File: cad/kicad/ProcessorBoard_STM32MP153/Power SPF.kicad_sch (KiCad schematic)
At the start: 8 parts

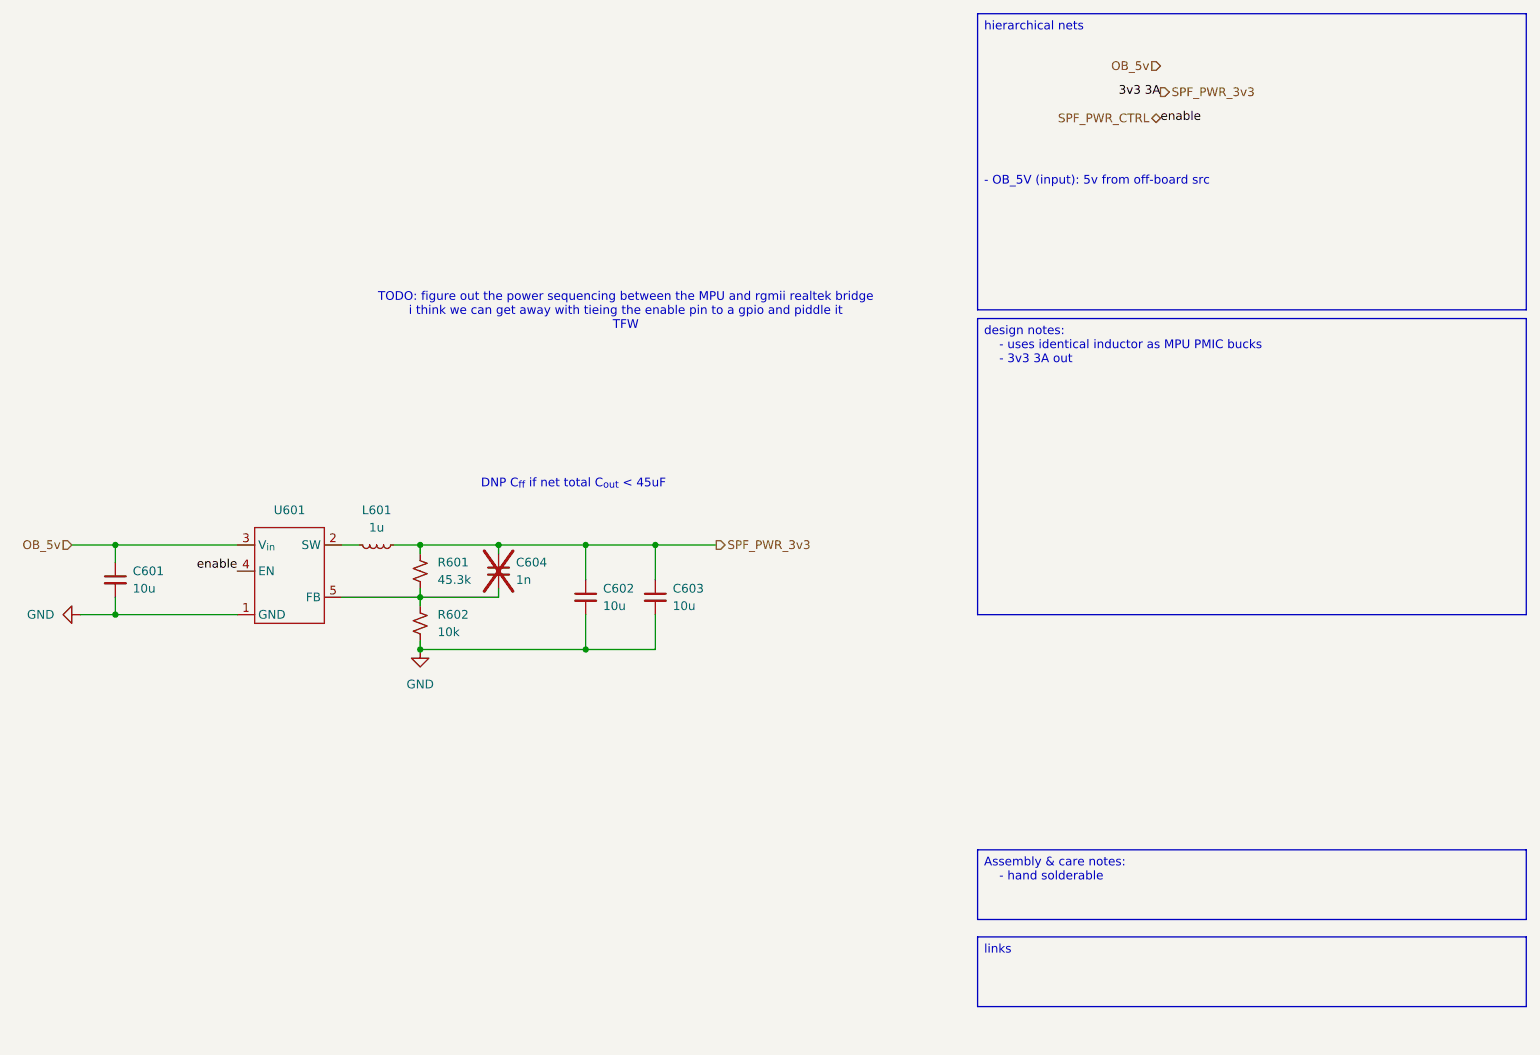
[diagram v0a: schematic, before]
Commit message: new ram
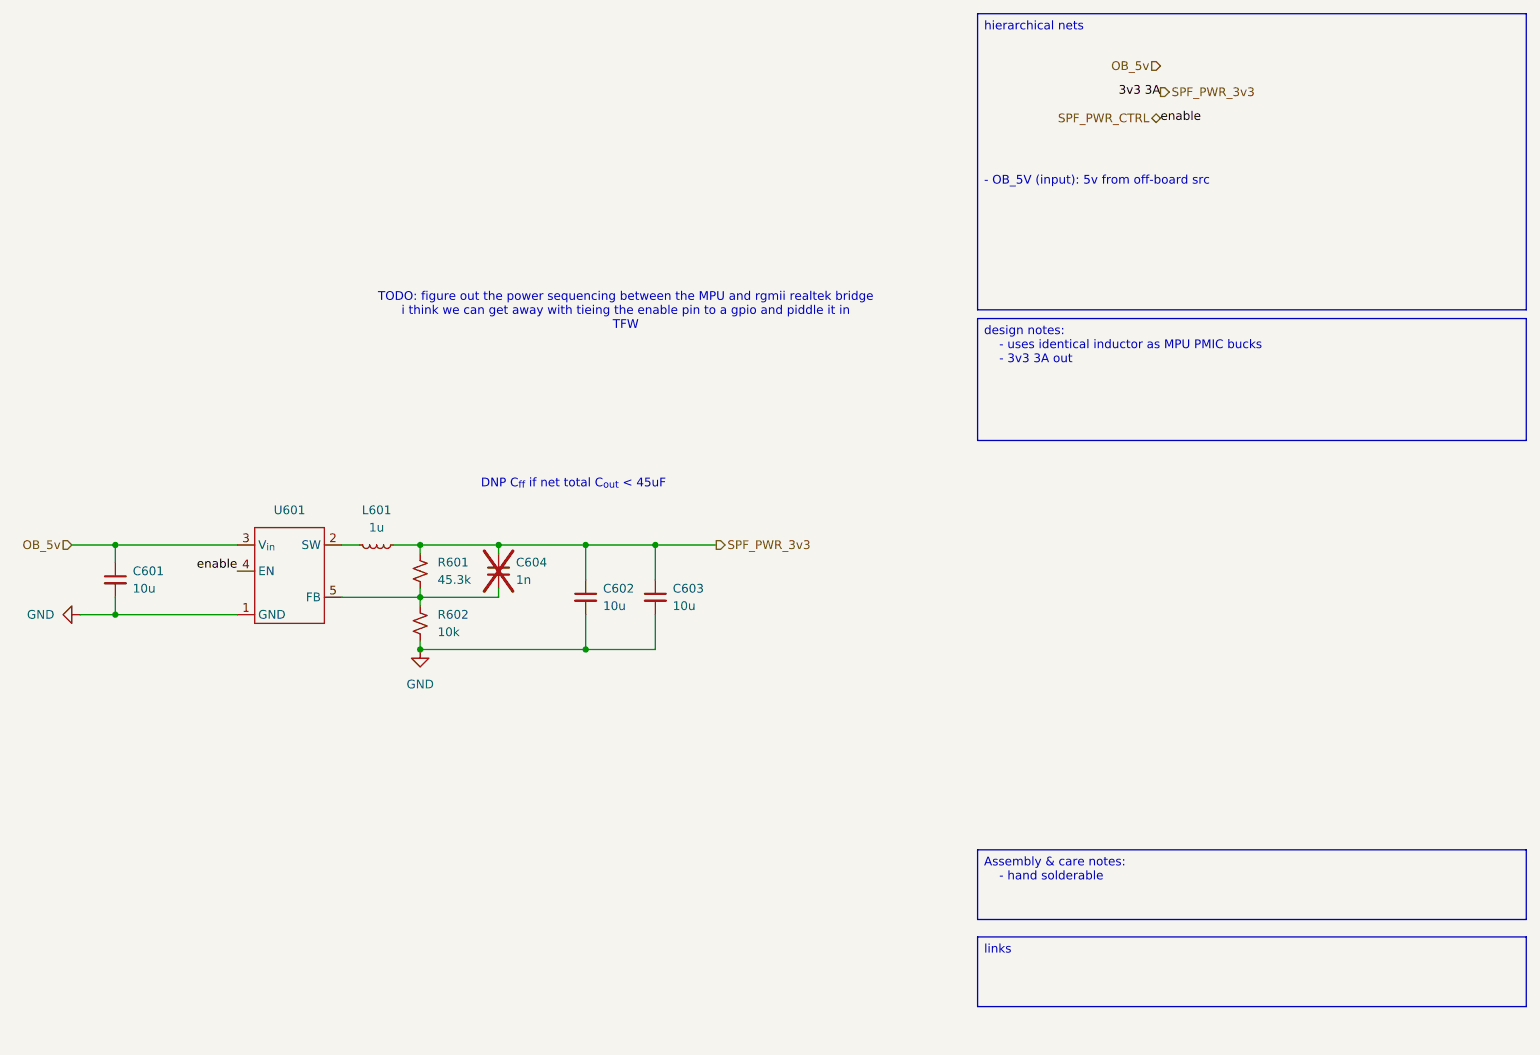
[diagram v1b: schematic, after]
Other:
- note added: "TODO: figure out the power sequencing between the MPU and rgmii realtek bridge i think we can get away with tieing the enable pin to a gpio and piddle it in TFW"
- note removed: "TODO: figure out the power sequencing between the MPU and rgmii realtek bridge i think we can get away with tieing the enable pin to a gpio and piddle it TFW"
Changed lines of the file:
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@@
 		)
 	)
-	(text "TODO: figure out the power sequencing between the MPU and rgmii realtek bridge\ni think we can get away with tieing the enable pin to a gpio and piddle it \nTFW"
+	(text "TODO: figure out the power sequencing between the MPU and rgmii realtek bridge\ni think we can get away with tieing the enable pin to a gpio and piddle it in\nTFW"
 		(exclude_from_sim no)
 		(at 151.892 57.404 0)
@@
 		(exclude_from_sim no)
 		(at 203.2 58.42 0)
-		(size 80.01 43.18)
+		(size 80.01 17.78)
 		(margins 0.9398 0.9398 0.9398 0.9398)
 		(stroke

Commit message: realtek bridge thing somewhat more wired
apparently the proper term for via skimping and what not is NFPR (non functional pad removal). all my homies love NFPR. so it is possible to route 0.5mm bga. still fighting the dog but at least cant bring it to another layer
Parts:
- removed C604: 1n, Capacitor_SMD:C_01005_0402Metric_Pad0.57x0.30mm_HandSolder, symbol Device:C_Small
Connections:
- no-connect marks 0 -> 2
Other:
- note added: "C_{ff} needed if C_{out} > 45uF"
- note removed: "DNP C_{ff} if net total C_{out} < 45uF"
- moved on the sheet: C601, C602, C603, L601, R601, R602, U601

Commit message: boo womp 10000
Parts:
- C601, C602, C603, L601, R601, R602, U601: now not fitted; now left out of the parts list
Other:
- note added: "TODO: check if theres power squencing between the SFP bridge IC and the MPU"
- note removed: "TODO: figure out the power sequencing between the MPU and rgmii realtek bridge i think we can get away with tieing the enable pin to a gpio and piddle it in TFW"
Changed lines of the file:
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@@
 		)
 	)
-	(text "TODO: figure out the power sequencing between the MPU and rgmii realtek bridge\ni think we can get away with tieing the enable pin to a gpio and piddle it in\nTFW"
+	(text "TODO: check if theres power squencing between the SFP bridge IC and the MPU"
 		(exclude_from_sim no)
-		(at 125.984 73.406 0)
+		(at 126.746 84.582 0)
 		(effects
 			(font
@@
 		(body_style 1)
 		(exclude_from_sim no)
-		(in_bom yes)
-		(on_board yes)
-		(in_pos_files yes)
-		(dnp no)
+		(in_bom no)
+		(on_board no)
+		(in_pos_files no)
+		(dnp yes)
 		(fields_autoplaced yes)
 		(property "Reference" "C601"
@@
 		(body_style 1)
 		(exclude_from_sim no)
-		(in_bom yes)
-		(on_board yes)
-		(in_pos_files yes)
-		(dnp no)
+		(in_bom no)
+		(on_board no)
+		(in_pos_files no)
+		(dnp yes)
 		(fields_autoplaced yes)
 		(property "Reference" "#PWR0602"
@@
 		(body_style 1)
 		(exclude_from_sim no)
-		(in_bom yes)
-		(on_board yes)
-		(in_pos_files yes)
-		(dnp no)
+		(in_bom no)
+		(on_board no)
+		(in_pos_files no)
+		(dnp yes)
 		(fields_autoplaced yes)
 		(property "Reference" "L601"
@@
 		(body_style 1)
 		(exclude_from_sim no)
-		(in_bom yes)
-		(on_board yes)
-		(in_pos_files yes)
-		(dnp no)
+		(in_bom no)
+		(on_board no)
+		(in_pos_files no)
+		(dnp yes)
 		(fields_autoplaced yes)
 		(property "Reference" "R601"
@@
 		(body_style 1)
 		(exclude_from_sim no)
-		(in_bom yes)
-		(on_board yes)
-		(in_pos_files yes)
-		(dnp no)
+		(in_bom no)
+		(on_board no)
+		(in_pos_files no)
+		(dnp yes)
 		(fields_autoplaced yes)
 		(property "Reference" "C602"
@@
 		(body_style 1)
 		(exclude_from_sim no)
-		(in_bom yes)
-		(on_board yes)
-		(in_pos_files yes)
-		(dnp no)
+		(in_bom no)
+		(on_board no)
+		(in_pos_files no)
+		(dnp yes)
 		(fields_autoplaced yes)
 		(property "Reference" "R602"
@@
 		(body_style 1)
 		(exclude_from_sim no)
-		(in_bom yes)
-		(on_board yes)
-		(in_pos_files yes)
-		(dnp no)
+		(in_bom no)
+		(on_board no)
+		(in_pos_files no)
+		(dnp yes)
 		(fields_autoplaced yes)
 		(property "Reference" "U601"
@@
 		(body_style 1)
 		(exclude_from_sim no)
-		(in_bom yes)
-		(on_board yes)
-		(in_pos_files yes)
-		(dnp no)
+		(in_bom no)
+		(on_board no)
+		(in_pos_files no)
+		(dnp yes)
 		(fields_autoplaced yes)
 		(property "Reference" "C603"
